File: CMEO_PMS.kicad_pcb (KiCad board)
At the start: 2 copper layers, 62.2 x 25.2 mm, 18 parts, among them J1 Conn_01x02, J2 Conn_01x02, T1 B78310P8078A002

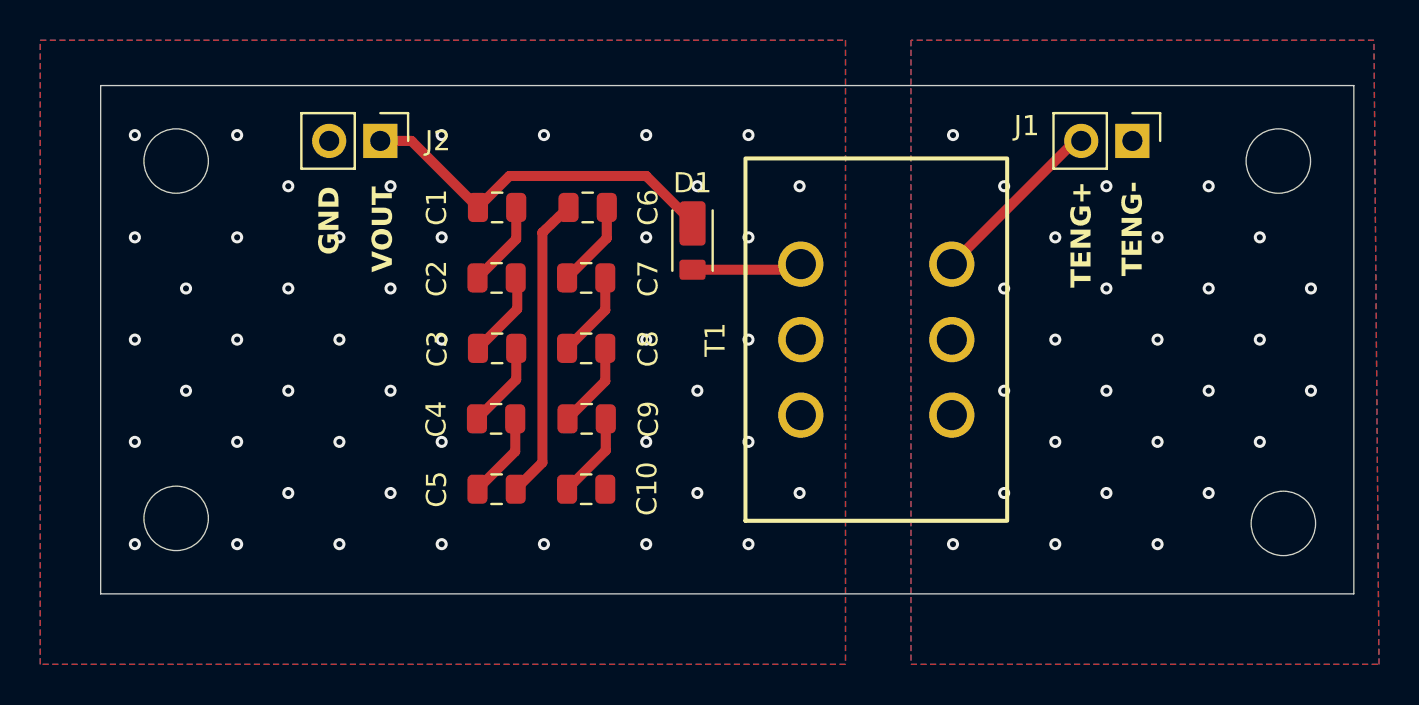
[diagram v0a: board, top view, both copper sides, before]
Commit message: CMEO_PMS Board V1.0 REV B
- Separated input and output headers to reduce risk of high voltage breakdown
- Increased fill gap to 2mm to reduce risk of high voltage breakdown
- Changed diode to THT for easier soldering
- Changed capacitor to 10uF, 400V limit. increase in capacitance is to better act as a battery for power purposes
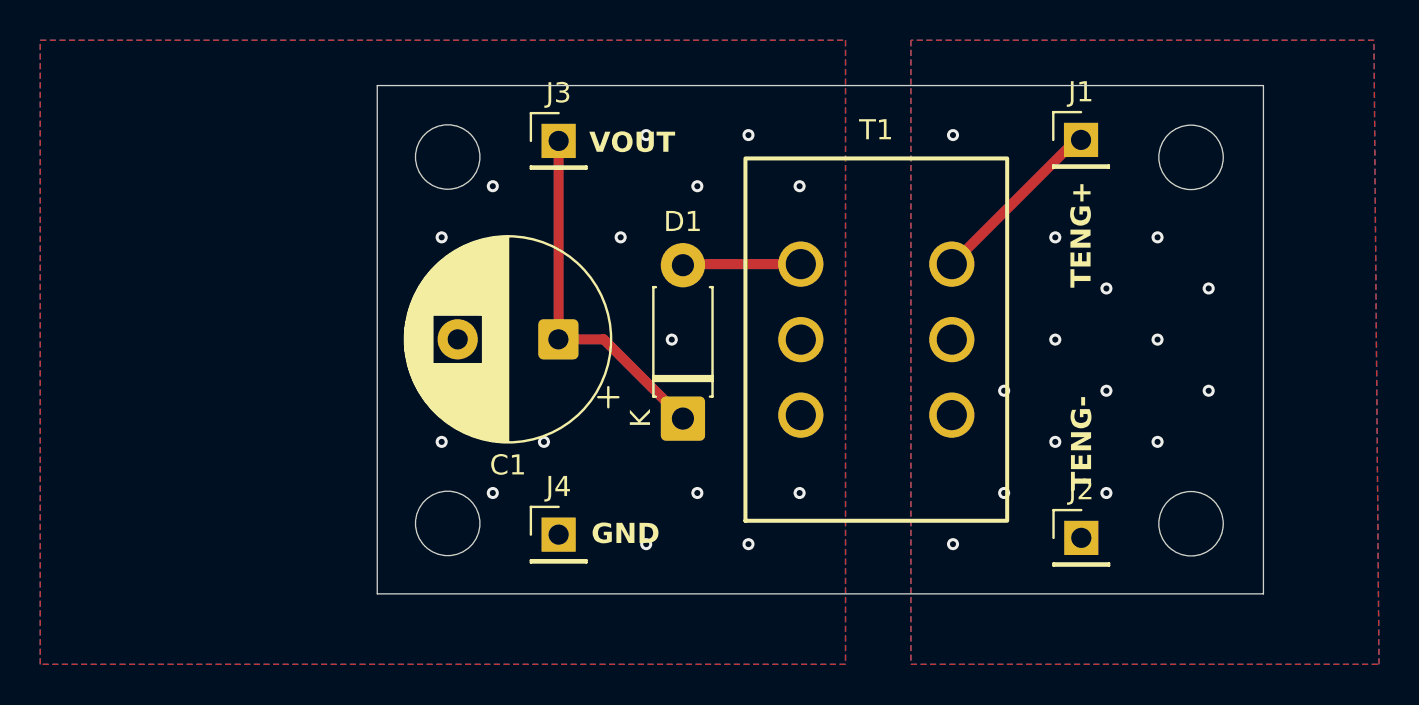
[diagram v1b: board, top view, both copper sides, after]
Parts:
- removed C10, C2, C3, C4, C5, C6, C7, C8, C9: 10nF, Capacitor_SMD:C_0805_2012Metric
- added J3: Conn_01x01, Connector_PinHeader_2.54mm:PinHeader_1x01_P2.54mm_Vertical, F.Cu at (160.8, 61.2)
- added J4: Conn_01x01, Connector_PinHeader_2.54mm:PinHeader_1x01_P2.54mm_Vertical, F.Cu at (160.8, 80.8)
- C1: value 10nF -> 10uF; footprint Capacitor_SMD:C_0805_2012Metric -> Capacitor_THT:CP_Radial_D10.0mm_P5.00mm
- D1: value D -> 1N4004RLG; footprint CMEO_PMS:DFLR1400-7 -> Diode_THT:D_DO-41_SOD81_P7.62mm_Horizontal
- J1, J2: value Conn_01x02 -> Conn_01x01; footprint Connector_PinHeader_2.54mm:PinHeader_1x02_P2.54mm_Vertical -> Connector_PinHeader_2.54mm:PinHeader_1x01_P2.54mm_Vertical
- moved J2 40.0 mm to (186.7, 81.0), turned to 0 degrees
- moved H4 13.5 mm to (155.2, 80.2)
- moved H2 13.5 mm to (155.2, 62.0)
- moved D1 8.86 mm to (166.9, 75.0)
- moved C1 7.22 mm to (160.7, 71.1), turned to 180 degrees
- moved H3 4.59 mm to (192.2, 80.3)
- moved H1 4.34 mm to (192.2, 62.1)
- moved J1 2.55 mm to (186.7, 61.2), turned to 0 degrees
- renumbered H3 to H2, H2 to H3
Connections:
- C1 pad 2: Net-(C1-Pad2) -> GND2
- J1 pad 1: GND1 -> /MS_RTENG_OUT
- J2 pad 1: /V_OUT -> GND1
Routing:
- net Net-(C5-Pad2): track 15.1 -> 0.00 mm
- net Net-(C2-Pad2): track 4.38 -> 0.00 mm
- net Net-(C6-Pad2): track 4.32 -> 0.00 mm
- net Net-(C3-Pad2): track 4.31 -> 0.00 mm
- net Net-(C1-Pad2): track 4.30 -> 0.00 mm
- net Net-(C10-Pad1): track 4.29 -> 0.00 mm
- net Net-(C7-Pad2): track 4.29 -> 0.00 mm
- net Net-(C8-Pad2): track 4.28 -> 0.00 mm
- net Net-(C4-Pad2): track 4.27 -> 0.00 mm
- net /V_OUT: track 18.5 -> 17.7 mm
- net GND2: vias 46 -> 15
- net GND1: vias 27 -> 15
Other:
- board size 62.2 x 25.2 mm -> 44 x 25.2 mm

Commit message: Fixed Silkscreen errors
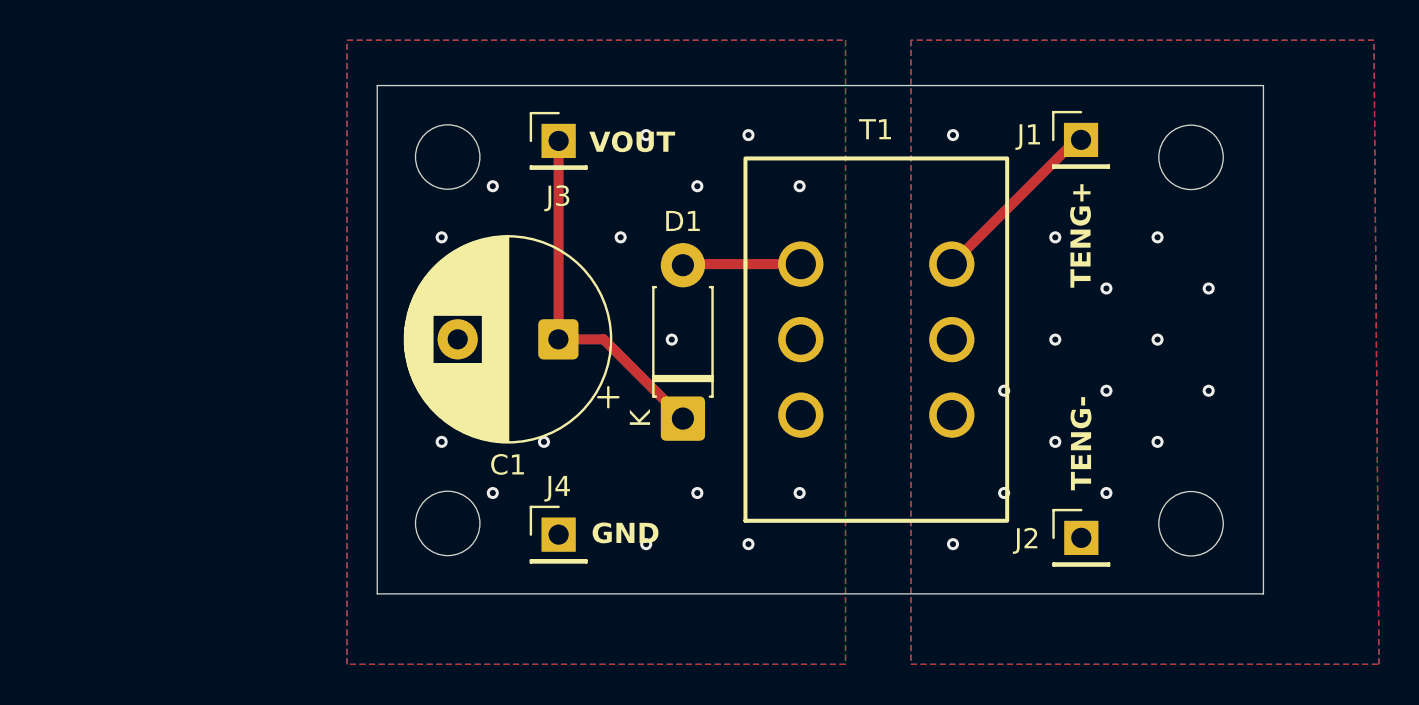
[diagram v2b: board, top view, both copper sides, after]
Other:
- board text added: "V1.0 REV B PD 05/18 Ryan Wang"
- board text removed: "V1.0 REV A PD 05/18 Ryan Wang"
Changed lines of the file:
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@@
 		(tags "Through hole pin header THT 1x01 2.54mm single row")
 		(property "Reference" "J1"
-			(at 0 -2.38 0)
+			(at -2.55 -0.24 0)
 			(layer "F.SilkS")
 			(effects
@@
 		(tags "Through hole pin header THT 1x01 2.54mm single row")
 		(property "Reference" "J2"
-			(at 0 -2.38 0)
+			(at -2.690296 0.058106 0)
 			(layer "F.SilkS")
 			(effects
@@
 		(tags "Through hole pin header THT 1x01 2.54mm single row")
 		(property "Reference" "J3"
-			(at 0 -2.38 0)
+			(at 0 2.758 0)
 			(layer "F.SilkS")
 			(effects
@@
 		)
 	)
-	(gr_text "V1.0 REV A\nPD 05/18\nRyan Wang"
+	(gr_text "V1.0 REV B\nPD 05/18\nRyan Wang"
 		(at 194.06 74.596 0)
 		(layer "B.SilkS")
@@
 			(justify left bottom mirror)
 		)
-		(render_cache "V1.0 REV A\nPD 05/18\nRyan Wang" 0
+		(render_cache "V1.0 REV B\nPD 05/18\nRyan Wang" 0
 			(polygon
 				(pts
@@
 			(polygon
 				(pts
-					(xy 187.581702 71.066) (xy 187.367196 71.066) (xy 187.28452 70.839342) (xy 186.884267 70.839342)
-					(xy 186.796828 71.066) (xy 186.576826 71.066) (xy 186.734412 70.671303) (xy 186.949113 70.671303)
-					(xy 187.22236 70.671303) (xy 187.08711 70.296146) (xy 186.949113 70.671303) (xy 186.734412 70.671303)
-					(xy 186.977812 70.061673) (xy 187.191646 70.061673)
+					(xy 187.426486 71.066) (xy 187.085645 71.066) (xy 186.909625 71.063051) (xy 186.841769 71.059161)
+					(xy 186.789263 71.04948) (xy 186.74445 71.033473) (xy 186.706153 71.011533) (xy 186.672348 70.983082)
+					(xy 186.643499 70.948785) (xy 186.619385 70.907974) (xy 186.601603 70.863916) (xy 186.591117 70.819623)
+					(xy 186.587634 70.774618) (xy 186.588508 70.765886) (xy 186.796645 70.765886) (xy 186.800084 70.800619)
+					(xy 186.809697 70.828703) (xy 186.825038 70.851554) (xy 186.857225 70.877401) (xy 186.898433 70.891793)
+					(xy 186.937562 70.895906) (xy 187.037102 70.89796) (xy 187.224253 70.89796) (xy 187.224253 70.628316)
+					(xy 187.060976 70.628316) (xy 186.934942 70.633035) (xy 186.881702 70.642788) (xy 186.844723 70.661893)
+					(xy 186.818504 70.688889) (xy 186.802341 70.723149) (xy 186.796645 70.765886) (xy 186.588508 70.765886)
+					(xy 186.593277 70.718245) (xy 186.609684 70.668202) (xy 186.636849 70.623126) (xy 186.673333 70.585151)
+					(xy 186.71962 70.554744) (xy 186.777533 70.531901) (xy 186.73704 70.508856) (xy 186.702986 70.479581)
+					(xy 186.674706 70.443608) (xy 186.653611 70.402996) (xy 186.641036 70.360126) (xy 186.639478 70.343285)
+					(xy 186.833525 70.343285) (xy 186.837031 70.374249) (xy 186.846986 70.399818) (xy 186.863262 70.421198)
+					(xy 186.89734 70.444379) (xy 186.944839 70.456858) (xy 187.091751 70.460277) (xy 187.224253 70.460277)
+					(xy 187.224253 70.229712) (xy 187.108115 70.229712) (xy 186.935314 70.233131) (xy 186.9029 70.240231)
+					(xy 186.878039 70.252036) (xy 186.859171 70.26818) (xy 186.840237 70.300531) (xy 186.833525 70.343285)
+					(xy 186.639478 70.343285) (xy 186.636788 70.31422) (xy 186.640303 70.271715) (xy 186.650585 70.232828)
+					(xy 186.667562 70.196861) (xy 186.702522 70.149273) (xy 186.744377 70.113025) (xy 186.793181 70.087072)
+					(xy 186.848913 70.071626) (xy 186.914881 70.064609) (xy 187.026172 70.061673) (xy 187.426486 70.061673)
 				)
 			)
@@
 		(layer "F.Cu")
 		(hatch none 0.1)
-		(priority 30004)
+		(priority 30005)
 		(attr
 			(teardrop
@@
 		(layer "F.Cu")
 		(hatch none 0.1)
-		(priority 30005)
+		(priority 30004)
 		(attr
 			(teardrop
@@
 		(polygon
 			(pts
-				(xy 135 56.25) (xy 175 56.25) (xy 175 87.25) (xy 135 87.25)
+				(xy 150.24 56.25) (xy 175 56.25) (xy 175 87.25) (xy 150.24 87.25)
 			)
 		)
